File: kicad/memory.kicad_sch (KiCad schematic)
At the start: 12 parts, among them J8 Molex 87715-9106, U11 ATF22V10C-7PX, U12 ATF22V10C-7PX, U25 CD74ACT273E, U31 AS7C256C-15PCN, U32 AS7C256C-15PCN

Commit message: Kit footprints: DIP sockets with puller room and part number, resistors with value
Justin: put the chip-puller room in the socket footprints (User.Eco1,
2.5 mm past each end) and the part number in silkscreen between the pin
rows; resistors get their value in silkscreen on the body. New
gen_kicad_kit_footprints.py derives them from KiCad's stock footprints;
schematic, symbols, BOM and PDFs now name them. The board file is left
as is (Justin is editing it): Update PCB from Schematic swaps them in.

Co-Authored-By: Claude Opus 5.5 (1M context) <noreply@anthropic.com>
Claude-Session: https://claude.ai/code/session_01JnVuvUvdWezUUU6Sgmg16H
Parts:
- R13: footprint Resistor_THT:R_Axial_DIN0207_L6.3mm_D2.5mm_P10.16mm_Horizontal -> placard:R_Axial_DIN0207_L6.3mm_D2.5mm_P10.16mm_Horizontal_Value
- U11, U12: footprint Package_DIP:DIP-24_W7.62mm -> placard:DIP-24_W7.62mm_Socket_Puller
- U25: footprint Package_DIP:DIP-20_W7.62mm -> placard:DIP-20_W7.62mm_Socket_Puller
- U31, U32: footprint Package_DIP:DIP-28_W7.62mm -> placard:DIP-28_W7.62mm_Socket_Puller

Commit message: BOM/schematic: stocked substitutes from the first parts order
D18 Kingbright WP7113ID (LTL2R3KRD-EM out of stock), 100n TDK
FG28X7R1H104KNT00 (KEMET C320C104 $0.66 at Mouser), C45 TDK
FG24C0G1H153JNT06 (KEMET non-stocked), Vishay BAT85S-TAP and
1N4148-TAP, MF-RG300-0, USB4125-GF-A-0190; Mouser prices re-checked.

Co-Authored-By: Claude Opus 5.5 (1M context) <noreply@anthropic.com>
Claude-Session: https://claude.ai/code/session_017y5UgjExE8oeP7QrfvhCzb
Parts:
- C11, C12, C25, C31, C32: MPN C320C104K5R5TA -> FG28X7R1H104KNT00; Manufacturer KEMET -> TDK

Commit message: Schematic: draw the /WE pull-up as R63 (memory sheet)
Memory control rev 09 lets go of /WE while RUN is low; the 10k pull-up was
only a BOM line.  Now R63 on the memory sheet, in the BOM as a normal part.

Co-Authored-By: Claude Opus 5.5 (1M context) <noreply@anthropic.com>
Claude-Session: https://claude.ai/code/session_016q7L8WUy2bLsrwHss8WZwY
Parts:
- added R63: 10k, placard:R_Axial_DIN0207_L6.3mm_D2.5mm_P10.16mm_Horizontal_Value, symbol placard_std:R_US
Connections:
- net +5V: now also R63.1
- net ~{WE}: now also R63.2
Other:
- note added: "RUN low (cartridge loading): /ROM_OE held off, map register clear (all ROM), /WE let go (R63)."
- note removed: "RUN low (cartridge loading): /ROM_OE held off, map register clear (all ROM)."
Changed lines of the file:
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@@
   (wire (pts (xy 208.28 246.38) (xy 248.92 246.38)) (stroke (width 0) (type default)))
   (wire (pts (xy 248.92 246.38) (xy 330.2 246.38)) (stroke (width 0) (type default)))
-  (wire (pts (xy 330.2 246.38) (xy 383.54 246.38)) (stroke (width 0) (type default)))
+  (wire (pts (xy 330.2 246.38) (xy 377.19 246.38)) (stroke (width 0) (type default)))
+  (wire (pts (xy 377.19 246.38) (xy 383.54 246.38)) (stroke (width 0) (type default)))
   (wire (pts (xy 210.82 248.92) (xy 246.38 248.92)) (stroke (width 0) (type default)))
   (wire (pts (xy 246.38 248.92) (xy 327.66 248.92)) (stroke (width 0) (type default)))
@@
   (symbol (lib_id "power:+5V") (at 271.78 125.73 0) (unit 1) (in_bom yes) (on_board yes) (dnp no) (property "Reference" "#PWR0723" (at 271.78 125.73 0) (effects (font (size 1.27 1.27)) hide)) (property "Value" "+5V" (at 271.78 119.38 0) (effects (font (size 2 2)))) (property "Footprint" "" (at 271.78 125.73 0) (effects (font (size 1.27 1.27)) hide)) (property "Datasheet" "" (at 271.78 125.73 0) (effects (font (size 1.27 1.27)) hide)) (pin "1") (instances (project "placard" (path "/e3450542-4ffc-59d4-a4a7-45636233928a/be6ca3b6-de05-5292-a0bc-3d79896ebd7e" (reference "#PWR0723") (unit 1)))))
   (symbol (lib_id "placard_std:R_US") (at 271.78 132.08 0) (unit 1) (in_bom yes) (on_board yes) (dnp no) (property "Reference" "R13" (at 273.78 131.58 0) (effects (font (size 2.54 2.54) bold) (justify left bottom))) (property "Value" "10k" (at 273.78 134.68 0) (effects (font (size 2 2)) (justify left top))) (property "Footprint" "placard:R_Axial_DIN0207_L6.3mm_D2.5mm_P10.16mm_Horizontal_Value" (at 271.78 132.08 0) (effects (font (size 1.27 1.27)) hide)) (property "Datasheet" "~" (at 271.78 132.08 0) (effects (font (size 1.27 1.27)) hide)) (property "Manufacturer" "Yageo" (at 271.78 132.08 0) (effects (font (size 1.27 1.27)) hide)) (property "MPN" "MFR-25FBF52-10K" (at 271.78 132.08 0) (effects (font (size 1.27 1.27)) hide)) (pin "1") (pin "2") (instances (project "placard" (path "/e3450542-4ffc-59d4-a4a7-45636233928a/be6ca3b6-de05-5292-a0bc-3d79896ebd7e" (reference "R13") (unit 1)))))
+  (wire (pts (xy 377.19 238.76) (xy 377.19 236.22)) (stroke (width 0) (type default)))
+  (symbol (lib_id "power:+5V") (at 377.19 236.22 0) (unit 1) (in_bom yes) (on_board yes) (dnp no) (property "Reference" "#PWR0724" (at 377.19 236.22 0) (effects (font (size 1.27 1.27)) hide)) (property "Value" "+5V" (at 377.19 229.87 0) (effects (font (size 2 2)))) (property "Footprint" "" (at 377.19 236.22 0) (effects (font (size 1.27 1.27)) hide)) (property "Datasheet" "" (at 377.19 236.22 0) (effects (font (size 1.27 1.27)) hide)) (pin "1") (instances (project "placard" (path "/e3450542-4ffc-59d4-a4a7-45636233928a/be6ca3b6-de05-5292-a0bc-3d79896ebd7e" (reference "#PWR0724") (unit 1)))))
+  (symbol (lib_id "placard_std:R_US") (at 377.19 242.57 0) (unit 1) (in_bom yes) (on_board yes) (dnp no) (property "Reference" "R63" (at 367.03 241.3 0) (effects (font (size 2.54 2.54) bold) (justify left bottom))) (property "Value" "10k" (at 367.03 243.84 0) (effects (font (size 2 2)) (justify left top))) (property "Footprint" "placard:R_Axial_DIN0207_L6.3mm_D2.5mm_P10.16mm_Horizontal_Value" (at 377.19 242.57 0) (effects (font (size 1.27 1.27)) hide)) (property "Datasheet" "~" (at 377.19 242.57 0) (effects (font (size 1.27 1.27)) hide)) (property "Manufacturer" "Yageo" (at 377.19 242.57 0) (effects (font (size 1.27 1.27)) hide)) (property "MPN" "MFR-25FBF52-10K" (at 377.19 242.57 0) (effects (font (size 1.27 1.27)) hide)) (pin "1") (pin "2") (instances (project "placard" (path "/e3450542-4ffc-59d4-a4a7-45636233928a/be6ca3b6-de05-5292-a0bc-3d79896ebd7e" (reference "R63") (unit 1)))))
+  (junction (at 377.19 246.38) (diameter 0) (color 0 0 0 0))
   (text "Lower 32K: /CE = A15 (RAM U31, cartridge /CE_LO); upper: /CE_HI from U12." (at 20 258 0) (effects (font (size 2.2 2.2)) (justify left bottom)))
-  (text "RUN low (cartridge loading): /ROM_OE held off, map register clear (all ROM)." (at 20 261.52 0) (effects (font (size 2.2 2.2)) (justify left bottom)))
+  (text "RUN low (cartridge loading): /ROM_OE held off, map register clear (all ROM), /WE let go (R63)." (at 20 261.52 0) (effects (font (size 2.2 2.2)) (justify left bottom)))
   (text "/CART reads low with a cartridge in; nothing reads it yet.  21 spare contacts." (at 20 265.04 0) (effects (font (size 2.2 2.2)) (justify left bottom)))
   (wire (pts (xy 53.34 88.9) (xy 45.72 88.9)) (stroke (width 0) (type default)))

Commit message: Schematic: expansion slot contacts A8-B11 become BT1-BT8 (slot-1 boot)
Cards latch D7:D0, so the slots no longer carry SRC7:SRC0.  Slot 1's
BT1-BT5 carry STALL_IN, STALL_OUT, PC_ENABLE, PIXEL_ENABLE and /CART;
BT6-BT8 and slots 2-4's boot contacts are not connected
(EXPANSION.md, "Booting from slot 1").  Slots respaced to keep the labels
on the page.

Co-Authored-By: Claude Opus 5.5 (1M context) <noreply@anthropic.com>
Claude-Session: https://claude.ai/code/session_016q7L8WUy2bLsrwHss8WZwY
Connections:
- net ~{CART}: now reaches J8.B10 (/CART), R13.2
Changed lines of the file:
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@@
   (bus (pts (xy 284.48 86.36) (xy 284.48 88.9)) (stroke (width 0) (type default)))
   (bus (pts (xy 284.48 88.9) (xy 284.48 93.98)) (stroke (width 0) (type default)))
-  (wire (pts (xy 294.64 105.41) (xy 292.1 105.41)) (stroke (width 0) (type default)))
+  (wire (pts (xy 294.64 105.41) (xy 283.21 105.41)) (stroke (width 0) (type default)))
+  (wire (pts (xy 283.21 105.41) (xy 281.94 105.41)) (stroke (width 0) (type default)))
+  (global_label "~{CART}" (shape passive) (at 281.94 105.41 180) (fields_autoplaced) (effects (font (size 2 2)) (justify right)) (property "Intersheetrefs" "${INTERSHEET_REFS}" (at 281.94 105.41 0) (effects (font (size 2 2)) (justify left) hide)))
   (wire (pts (xy 345.44 54.61) (xy 353.06 54.61)) (stroke (width 0) (type default)))
   (label "D0" (at 345.44 54.61 0) (fields_autoplaced) (effects (font (size 2 2)) (justify left bottom)))
@@
   (bus (pts (xy 96.52 87.63) (xy 96.52 85.09)) (stroke (width 0) (type default)))
   (label "RAMSEL[0..7]" (at 96.52 85.09 90) (fields_autoplaced) (effects (font (size 2 2)) (justify left bottom)))
-  (wire (pts (xy 271.78 138.43) (xy 290.83 138.43)) (stroke (width 0) (type default)))
-  (wire (pts (xy 290.83 138.43) (xy 290.83 105.41)) (stroke (width 0) (type default)))
-  (wire (pts (xy 290.83 105.41) (xy 292.1 105.41)) (stroke (width 0) (type default)))
+  (wire (pts (xy 271.78 138.43) (xy 283.21 138.43)) (stroke (width 0) (type default)))
+  (wire (pts (xy 283.21 138.43) (xy 283.21 105.41)) (stroke (width 0) (type default)))
   (junction (at 96.52 88.9) (diameter 0) (color 0 0 0 0))
+  (junction (at 283.21 105.41) (diameter 0) (color 0 0 0 0))
 )

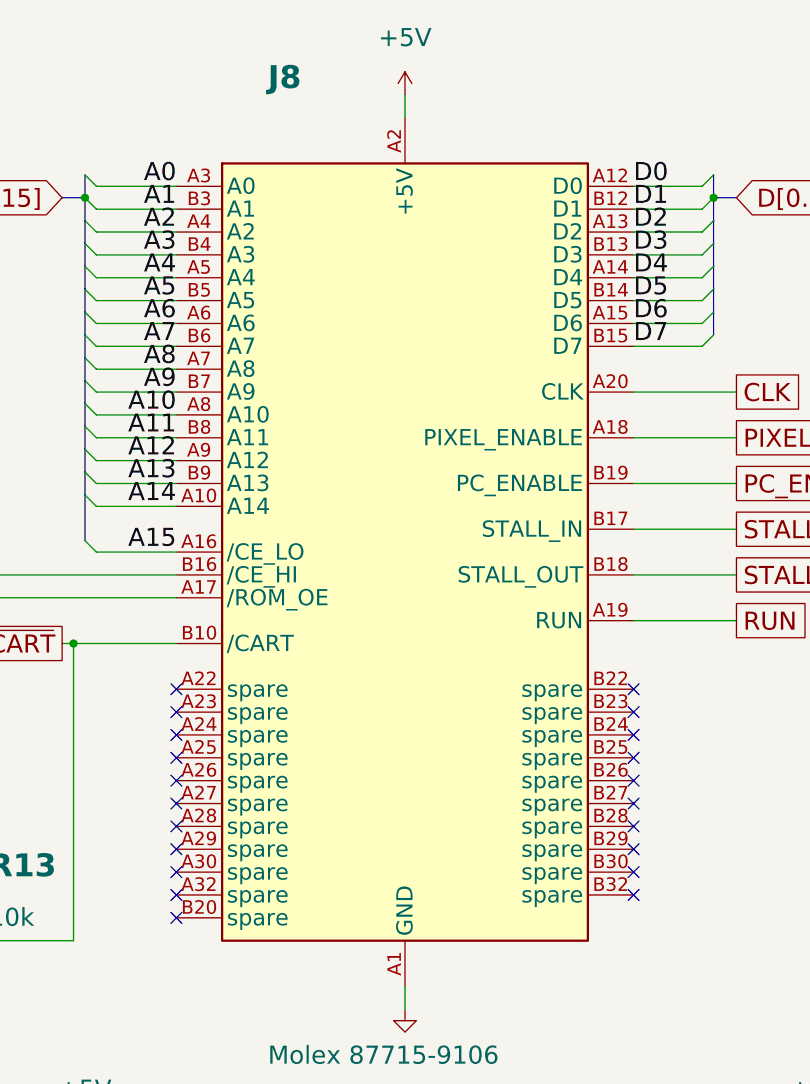
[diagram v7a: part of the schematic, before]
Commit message: Cartridge slot: contacts in cartridge chip-pin order for autorouting
The cartridge boards would not route with the address lines in bus
order on the connector (the loader PLD sits right behind the fingers).
Each side's signals now leave the fingers in the order of the chip pins
they reach, which lets both cartridge boards route on four layers.
One pinout table (CART_PINOUT) feeds J8 on the main board and J1 on the
cartridges; the slot symbol, every sheet, the PDFs, EXPANSION.md and
SCHEMATIC_PLAN.md follow.  The main board's J8 traces need rerouting.

Co-Authored-By: Claude Fable 5.1 <noreply@anthropic.com>
Claude-Session: https://claude.ai/code/session_017okF1JiLRNFTfH7Az85hff
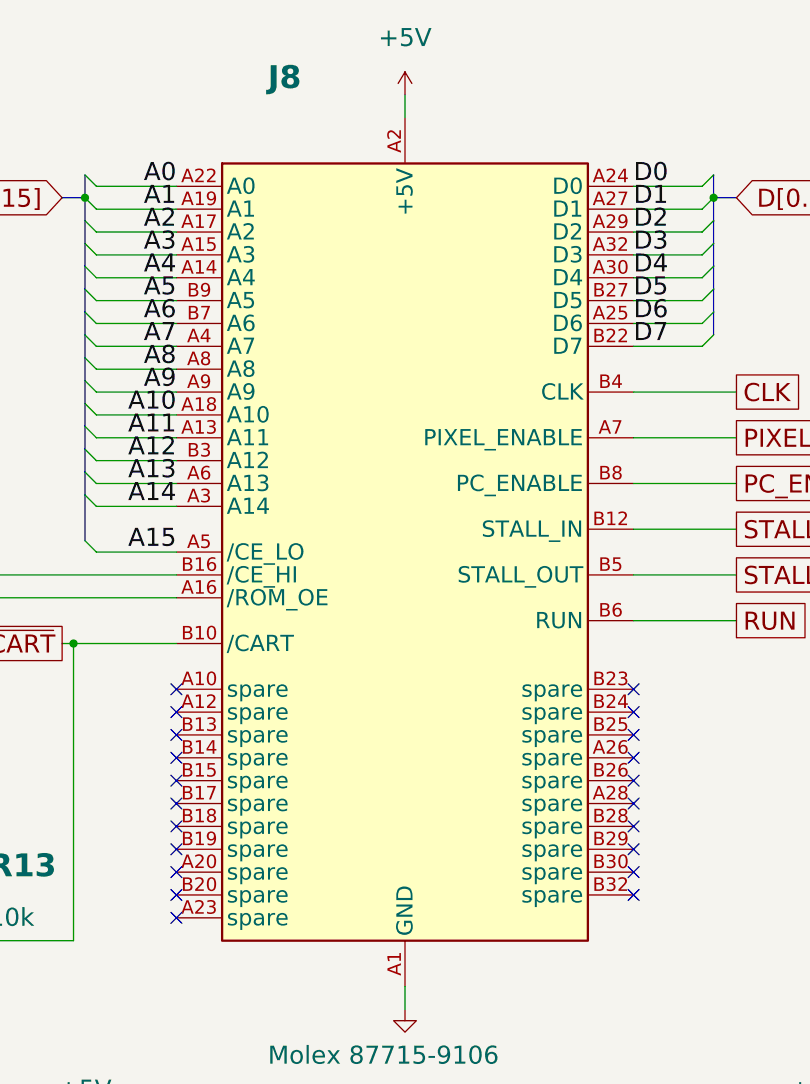
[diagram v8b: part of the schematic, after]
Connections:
- net A0: now also J8.A22 (A0); no longer J8.A3 (A0)
- net A1: now also J8.A19 (A1); no longer J8.B3 (A1)
- net A10: now also J8.A18 (A10); no longer J8.A8 (A10)
- net A11: now also J8.A13 (A11); no longer J8.B8 (A11)
- net A12: now also J8.B3 (A12); no longer J8.A9 (A12)
- net A13: now also J8.A6 (A13); no longer J8.B9 (A13)
- net A14: now also J8.A3 (A14); no longer J8.A10 (A14)
- net A15: now also J8.A5 (/CE_LO); no longer J8.A16 (/CE_LO)
- net A2: now also J8.A17 (A2); no longer J8.A4 (A2)
- net A3: now also J8.A15 (A3); no longer J8.B4 (A3)
- net A4: now also J8.A14 (A4); no longer J8.A5 (A4)
- net A5: now also J8.B9 (A5); no longer J8.B5 (A5)
- net A6: now also J8.B7 (A6); no longer J8.A6
- net A7: now also J8.A4 (A7); no longer J8.B6 (A7)
- net A8: now also J8.A8; no longer J8.A7 (A8)
- net A9: now also J8.A9; no longer J8.B7 (A9)
- net CLK: now also J8.B4 (CLK); no longer J8.A20 (CLK)
- net D0: now also J8.A24 (D0); no longer J8.A12 (D0)
- net D1: now also J8.A27 (D1); no longer J8.B12 (D1)
- net D2: now also J8.A29 (D2); no longer J8.A13 (D2)
- net D3: now also J8.A32 (D3); no longer J8.B13 (D3)
- net D4: now also J8.A30 (D4); no longer J8.A14 (D4)
- net D5: now also J8.B27 (D5); no longer J8.B14 (D5)
- net D6: now also J8.A25 (D6); no longer J8.A15 (D6)
- net D7: now also J8.B22 (D7); no longer J8.B15 (D7)
- net PC_ENABLE: now also J8.B8 (PC_ENABLE); no longer J8.B19 (PC_ENABLE)
- net PIXEL_ENABLE: now also J8.A7 (PIXEL_ENABLE); no longer J8.A18 (PIXEL_ENABLE)
- net RUN: now also J8.B6 (RUN); no longer J8.A19 (RUN)
- net STALL_IN: now also J8.B12 (STALL_IN); no longer J8.B17 (STALL_IN)
- net STALL_OUT: now also J8.B5 (STALL_OUT); no longer J8.B18 (STALL_OUT)
- net at U11.19 (/ROM_OE): now also J8.A16 (/ROM_OE); no longer J8.A17 (/ROM_OE)
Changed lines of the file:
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@@
 (kicad_sch (version 20230121) (generator eeschema)
   (paper "A3")
-  (title_block (title "Placard: Memory and I/O decode") (date "2026-10-25") (rev "1") (company "Placard computer") (comment 1 "Generated by src/scripts/gen_kicad_schematic.py; plan in docs/SCHEMATIC_PLAN.md") (comment 2 "Chip numbers U1-U42 = docs/CHIPS.md; decoupling Cn goes with Un"))
+  (title_block (title "Placard: Memory and I/O decode") (date "2026-10-26") (rev "1") (company "Placard computer") (comment 1 "Generated by src/scripts/gen_kicad_schematic.py; plan in docs/SCHEMATIC_PLAN.md") (comment 2 "Chip numbers U1-U42 = docs/CHIPS.md; decoupling Cn goes with Un"))
   (text "Memory and I/O decode" (at 15 22 0) (effects (font (size 6 6) bold) (justify left bottom)))
   (text "RAM, ROM cartridge slot, memory control, I/O decode, map register" (at 15 30 0) (effects (font (size 3 3)) (justify left bottom)))
@@
   (wire (pts (xy 320.04 143.51) (xy 320.04 146.05)) (stroke (width 0) (type default)))
   (symbol (lib_id "power:GND") (at 320.04 146.05 0) (unit 1) (in_bom yes) (on_board yes) (dnp no) (property "Reference" "#PWR0722" (at 320.04 146.05 0) (effects (font (size 1.27 1.27)) hide)) (property "Value" "GND" (at 320.04 152.4 0) (effects (font (size 2 2)) hide)) (property "Footprint" "" (at 320.04 146.05 0) (effects (font (size 1.27 1.27)) hide)) (property "Datasheet" "" (at 320.04 146.05 0) (effects (font (size 1.27 1.27)) hide)) (pin "1") (instances (project "placard" (path "/e3450542-4ffc-59d4-a4a7-45636233928a/be6ca3b6-de05-5292-a0bc-3d79896ebd7e" (reference "#PWR0722") (unit 1)))))
-  (symbol (lib_id "placard_parts:Cartridge_Slot") (at 320.04 95.25 0) (unit 1) (in_bom yes) (on_board yes) (dnp no) (property "Reference" "J8" (at 304.8 44 0) (effects (font (size 2.54 2.54) bold) (justify left bottom))) (property "Value" "Molex 87715-9106" (at 304.8 150 0) (effects (font (size 2 2)) (justify left top))) (property "Footprint" "placard:Molex_87715-9106_PCIe_x4_Vertical" (at 320.04 95.25 0) (effects (font (size 1.27 1.27)) hide)) (property "Datasheet" "~" (at 320.04 95.25 0) (effects (font (size 1.27 1.27)) hide)) (property "Manufacturer" "Molex" (at 320.04 95.25 0) (effects (font (size 1.27 1.27)) hide)) (property "MPN" "87715-9106" (at 320.04 95.25 0) (effects (font (size 1.27 1.27)) hide)) (pin "A3") (pin "B3") (pin "A4") (pin "B4") (pin "A5") (pin "B5") (pin "A6") (pin "B6") (pin "A7") (pin "B7") (pin "A8") (pin "B8") (pin "A9") (pin "B9") (pin "A10") (pin "A16") (pin "B16") (pin "A17") (pin "B10") (pin "A22") (pin "A23") (pin "A24") (pin "A25") (pin "A26") (pin "A27") (pin "A28") (pin "A29") (pin "A30") (pin "A32") (pin "B20") (pin "A12") (pin "B12") (pin "A13") (pin "B13") (pin "A14") (pin "B14") (pin "A15") (pin "B15") (pin "A20") (pin "A18") (pin "B19") (pin "B17") (pin "B18") (pin "A19") (pin "B22") (pin "B23") (pin "B24") (pin "B25") (pin "B26") (pin "B27") (pin "B28") (pin "B29") (pin "B30") (pin "B32") (pin "A2") (pin "B2") (pin "A1") (pin "B1") (pin "A11") (pin "B11") (pin "A21") (pin "B21") (pin "A31") (pin "B31") (instances (project "placard" (path "/e3450542-4ffc-59d4-a4a7-45636233928a/be6ca3b6-de05-5292-a0bc-3d79896ebd7e" (reference "J8") (unit 1)))))
+  (symbol (lib_id "placard_parts:Cartridge_Slot") (at 320.04 95.25 0) (unit 1) (in_bom yes) (on_board yes) (dnp no) (property "Reference" "J8" (at 304.8 44 0) (effects (font (size 2.54 2.54) bold) (justify left bottom))) (property "Value" "Molex 87715-9106" (at 304.8 150 0) (effects (font (size 2 2)) (justify left top))) (property "Footprint" "placard:Molex_87715-9106_PCIe_x4_Vertical" (at 320.04 95.25 0) (effects (font (size 1.27 1.27)) hide)) (property "Datasheet" "~" (at 320.04 95.25 0) (effects (font (size 1.27 1.27)) hide)) (property "Manufacturer" "Molex" (at 320.04 95.25 0) (effects (font (size 1.27 1.27)) hide)) (property "MPN" "87715-9106" (at 320.04 95.25 0) (effects (font (size 1.27 1.27)) hide)) (pin "A22") (pin "A19") (pin "A17") (pin "A15") (pin "A14") (pin "B9") (pin "B7") (pin "A4") (pin "A8") (pin "A9") (pin "A18") (pin "A13") (pin "B3") (pin "A6") (pin "A3") (pin "A5") (pin "B16") (pin "A16") (pin "B10") (pin "A10") (pin "A12") (pin "B13") (pin "B14") (pin "B15") (pin "B17") (pin "B18") (pin "B19") (pin "A20") (pin "B20") (pin "A23") (pin "A24") (pin "A27") (pin "A29") (pin "A32") (pin "A30") (pin "B27") (pin "A25") (pin "B22") (pin "B4") (pin "A7") (pin "B8") (pin "B12") (pin "B5") (pin "B6") (pin "B23") (pin "B24") (pin "B25") (pin "A26") (pin "B26") (pin "A28") (pin "B28") (pin "B29") (pin "B30") (pin "B32") (pin "A2") (pin "B2") (pin "A1") (pin "B1") (pin "A11") (pin "B11") (pin "A21") (pin "B21") (pin "A31") (pin "B31") (instances (project "placard" (path "/e3450542-4ffc-59d4-a4a7-45636233928a/be6ca3b6-de05-5292-a0bc-3d79896ebd7e" (reference "J8") (unit 1)))))
   (wire (pts (xy 177.8 76.2) (xy 208.28 76.2)) (stroke (width 0) (type default)))
   (wire (pts (xy 208.28 76.2) (xy 208.28 246.38)) (stroke (width 0) (type default)))
